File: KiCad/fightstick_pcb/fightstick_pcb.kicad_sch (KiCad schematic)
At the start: 93 parts, among them J1 USB_B_Micro, J2 Conn_01x02, J3 Conn_01x02, J4 Screw_Terminal_01x12, J5 Screw_Terminal_01x12, J6 Screw_Terminal_01x12, SW1 SW_Push, U1 SN74LVC1G14DBV, U10 SN74LVC1G14DBV, U11 SN74LVC1G14DBV, U12 SN74LVC1G14DBV, U13 SN74LVC1G14DBV, U14 SN74LVC1G14DBV, U15 SN74LVC1G14DBV, U2 SN74LVC1G14DBV, U3 NCP1117-3.3_SOT223, U4 W25Q128JVS, U5 SN74LVC1G14DBV, U6 SN74LVC1G14DBV, U7 SN74LVC1G14DBV, U8 SN74LVC1G14DBV, U9 RP2040, Y1 ABM8-272-T3

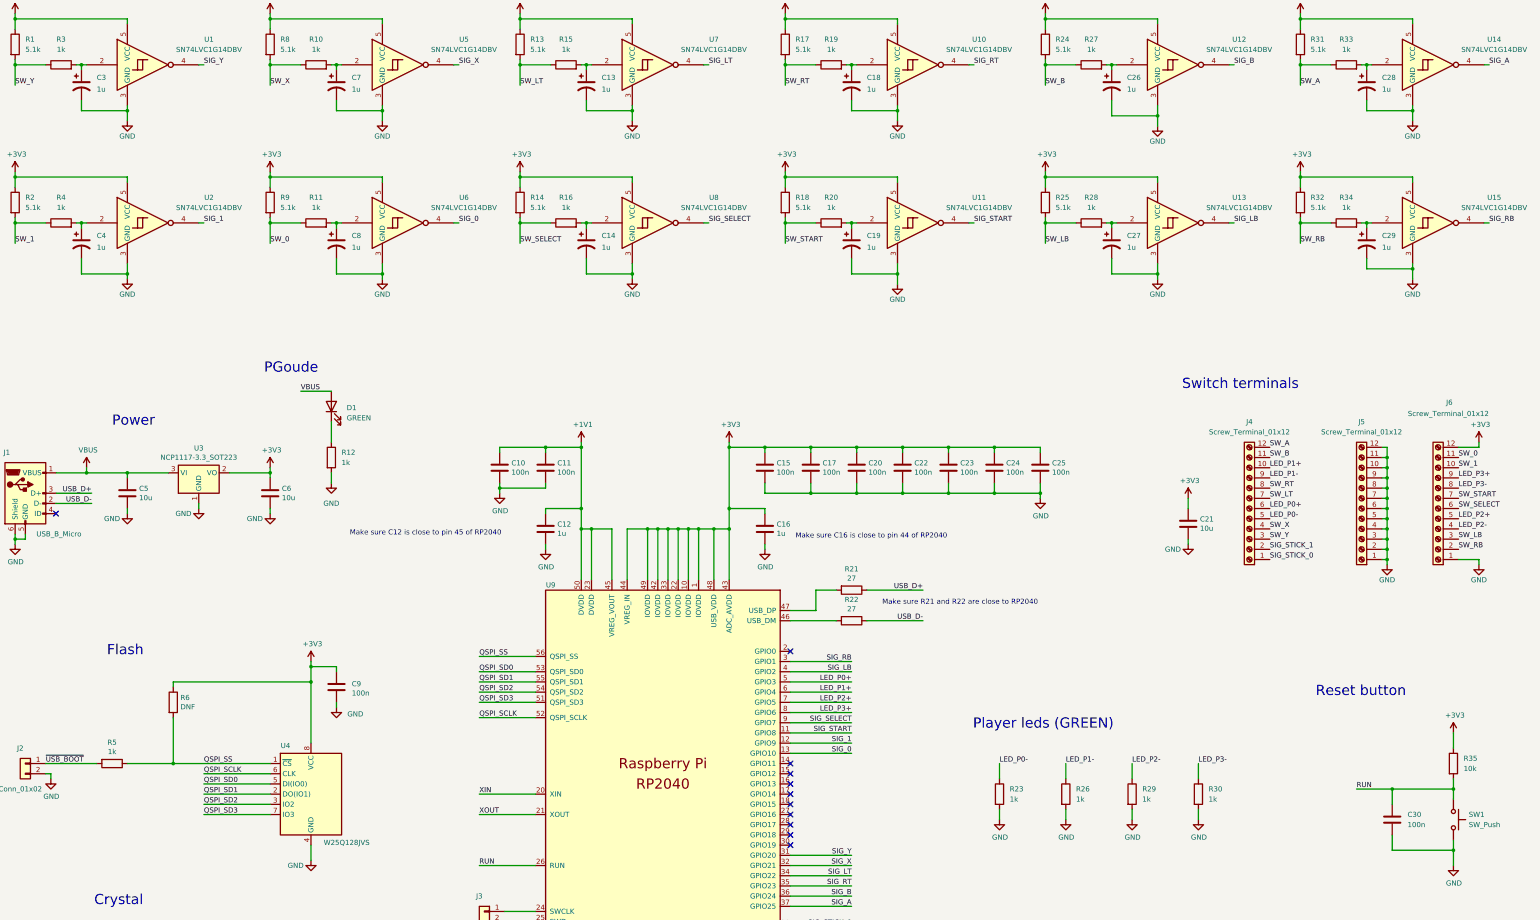
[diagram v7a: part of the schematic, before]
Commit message: PCB V1.1.0
Améliorations avec cap polarisés
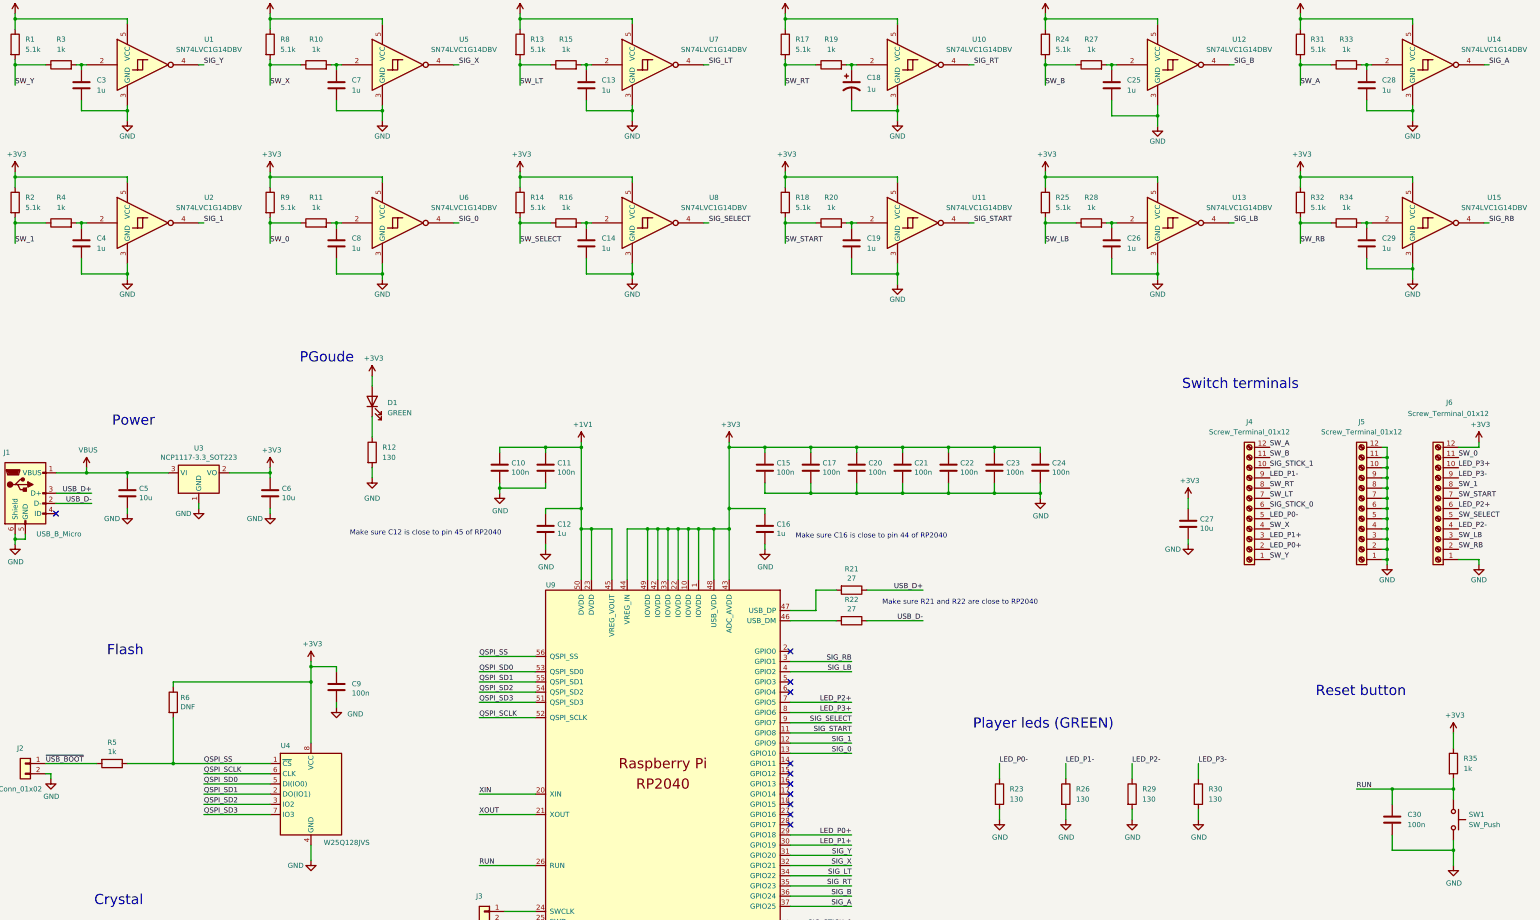
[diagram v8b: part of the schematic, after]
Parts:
- removed C13, C14, C19, C26, C27, C28, C29, C3, C4, C7, C8: 1u, Capacitor_SMD:CP_Elec_4x3, symbol Device:C_Polarized_US
- added C13, C14, C19, C25, C26, C28, C29, C3, C4, C7, C8: 1u, Capacitor_SMD:C_0805_2012Metric, symbol Device:C
- R12, R23, R26, R29, R30: value 1k -> 130
- R35: value 10k -> 1k
- renumbered C22 to C21, C23 to C22, C24 to C23, C25 to C24, C21 to C27
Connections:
- net +3V3: now also D1.2 (A)
- net GND: now also C13.2, C14.2, C19.2, C25.2, C26.2, C28.2, C29.2, C3.2, C4.2, C7.2, C8.2
- net LED_P0+: now also J4.2 (Pin_2), U9.29 (GPIO18); no longer J4.6 (Pin_6), U9.5 (GPIO3)
- net LED_P1+: now also J4.3 (Pin_3), U9.30 (GPIO19); no longer J4.10 (Pin_10), U9.6 (GPIO4)
- net LED_P2+: now also J6.6 (Pin_6); no longer J6.5 (Pin_5)
- net LED_P3+: now also J6.10 (Pin_10); no longer J6.9 (Pin_9)
- net LED_P3-: now also J6.9 (Pin_9); no longer J6.8 (Pin_8)
- net SIG_STICK_0: now also J4.6 (Pin_6); no longer J4.1 (Pin_1)
- net SIG_STICK_1: now also J4.10 (Pin_10); no longer J4.2 (Pin_2)
- net SW_1: now also J6.8 (Pin_8); no longer J6.10 (Pin_10)
- net SW_SELECT: now also J6.5 (Pin_5); no longer J6.6 (Pin_6)
- net SW_Y: now also J4.1 (Pin_1); no longer J4.3 (Pin_3)
- net VBUS: no longer D1.2 (A)
- net at R4.2, U2.2: now also C4.1
- net at R33.2, U14.2: now also C28.1
- net at R11.2, U6.2: now also C8.1
- net at R20.2, U11.2: now also C19.1
- net at R27.2, U12.2: now also C25.1
- net at R10.2, U5.2: now also C7.1
- net at R3.2, U1.2: now also C3.1
- net at R15.2, U7.2: now also C13.1
- net at R16.2, U8.2: now also C14.1
- net at R34.2, U15.2: now also C29.1
- net at R28.2, U13.2: now also C26.1
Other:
- moved on the sheet: D1, R12
